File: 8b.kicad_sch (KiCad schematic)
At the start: 51 parts, among them J1 AudioJack2, J11 AudioJack3, J2 AudioJack2, J3 AudioJack2, J4 AudioJack2, J5 AudioJack2, J6 AudioJack2, J7 AudioJack2, J8 AudioJack2, Q1 2N3904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

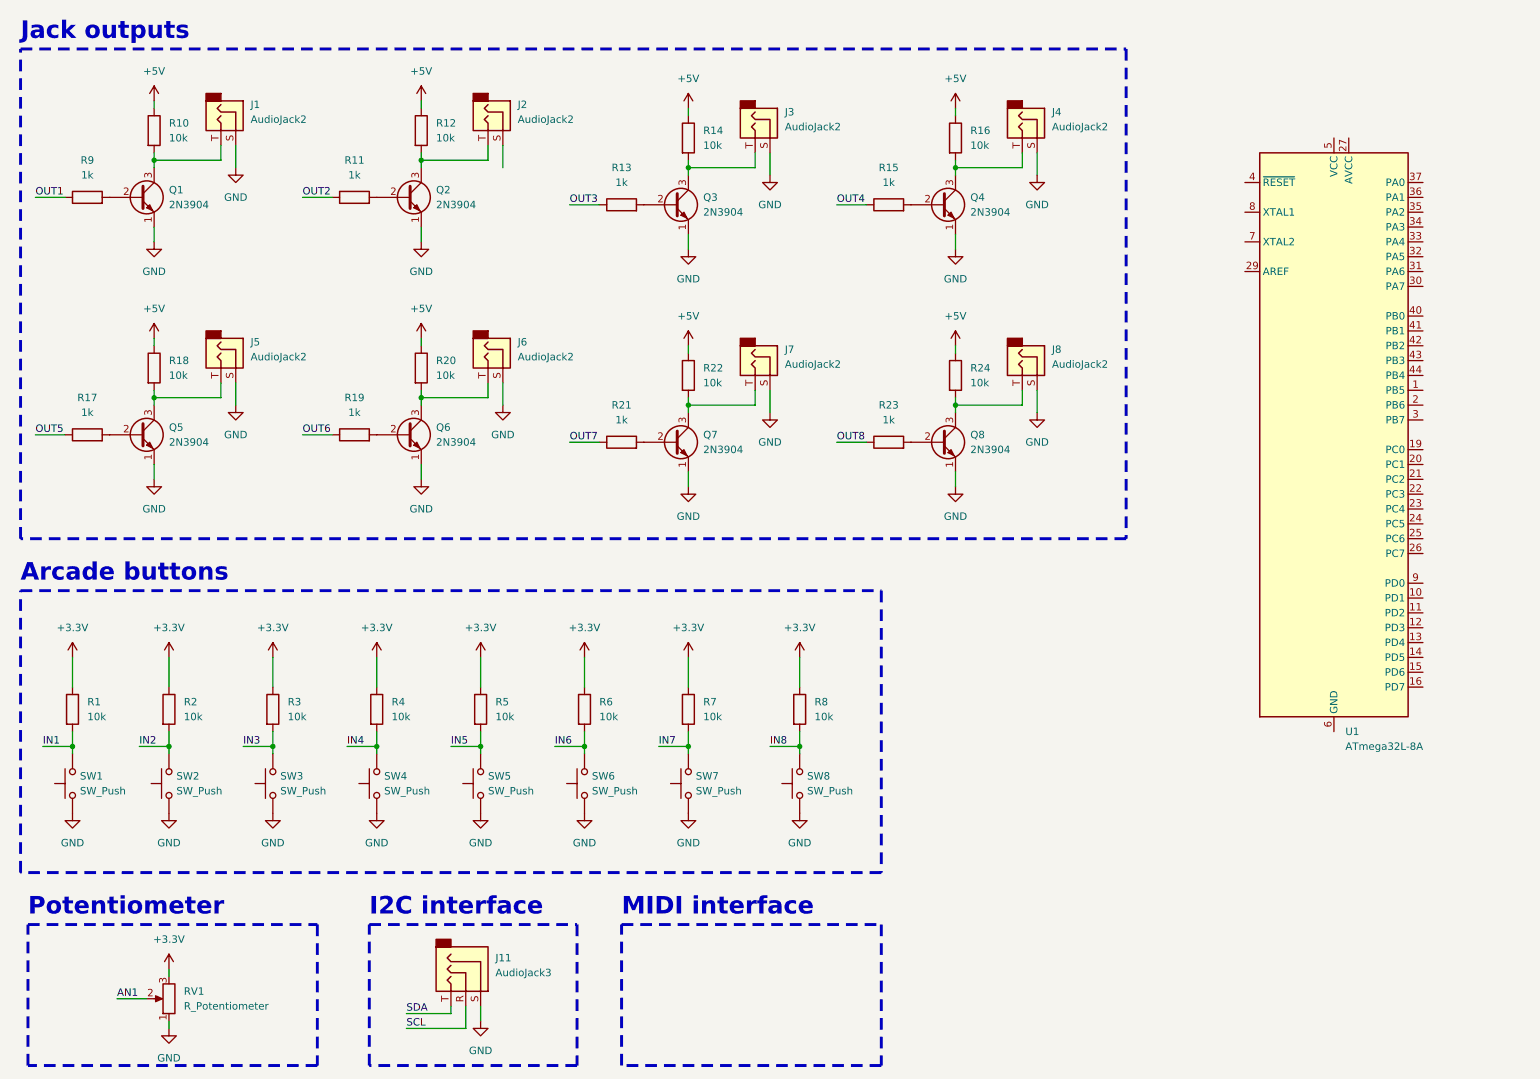
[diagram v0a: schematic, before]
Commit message: Add i2c interface & MIDI interface
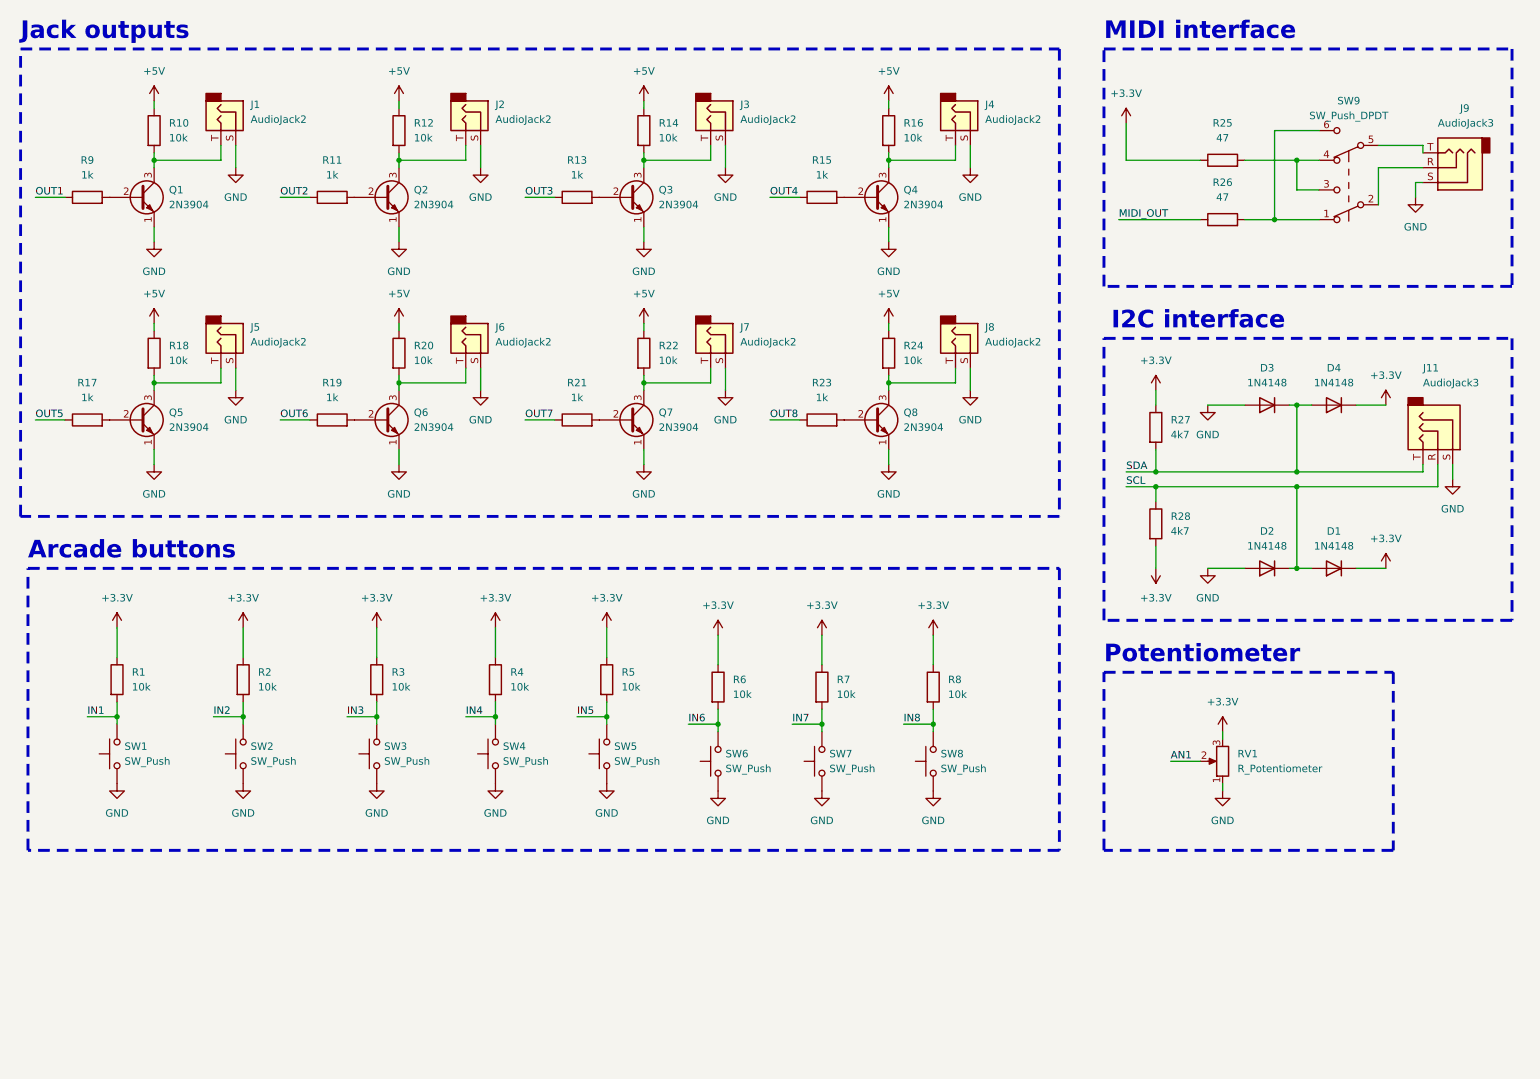
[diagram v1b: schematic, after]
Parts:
- removed U1: ATmega32L-8A, Package_QFP:TQFP-44_10x10mm_P0.8mm, symbol MCU_Microchip_ATmega:ATmega32L-8A
- added D1, D2, D3, D4: 1N4148, Diode_THT:D_DO-35_SOD27_P7.62mm_Horizontal, symbol Diode:1N4148
- added J9: AudioJack3, symbol Connector_Audio:AudioJack3
- added R25, R26: 47, symbol Device:R
- added R27, R28: 4k7, symbol Device:R
- added SW9: SW_Push_DPDT, symbol Switch:SW_Push_DPDT
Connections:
- net +3.3V: now also D1.1 (K), D4.1 (K), R25.1, R27.1, R28.2
- net GND: now also J2.S, D2.2 (A), D3.2 (A), J9.S
- net SCL: now also D1.2 (A), D2.1 (K), R28.1
- net SDA: now also D3.1 (K), D4.2 (A), R27.2
- new net: R26.2, SW9.1 (A), SW9.6 (C)
- new net: J9.R, SW9.2 (B)
- new net: J9.T, SW9.5 (B)
- new net: R25.2, SW9.3 (C), SW9.4 (A)
- new net MIDI_OUT: R26.1
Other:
- moved on the sheet: J11, J2, J3, J4, J5, J6, J7, J8, Q2, Q3, Q4, Q5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

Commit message: Update schem
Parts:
- added U1: Pico, RPi_Pico:RPi_Pico_SMD_TH, symbol RPi Pico:Pico
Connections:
- net +3.3V: now also R27.2, R28.1, U1.36 (3V3); no longer R27.1, R28.2
- net GND: now also U1.3 (GND), U1.42 (GND)
- net SCL: no longer R28.1
- net SDA: now also R27.1, R28.2; no longer R27.2
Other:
- note added: "Control"
- moved on the sheet: D1, D2, D3, D4, J11, J9, R1, R2, R25, R26, R27, R28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

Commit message: Update submodules & schematic
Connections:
- net +5V: now also U1.40 (VBUS)
- net AN1: now also U1.32 (GPIO27_ADC1)
- net GND: now also U1.13 (GND), U1.18 (GND), U1.23 (GND), U1.28 (GND), U1.33 (AGND), U1.38 (GND), U1.8 (GND)
- net IN1: now also U1.9 (GPIO6)
- net IN2: now also U1.10 (GPIO7)
- net IN3: now also U1.11 (GPIO8)
- net IN4: now also U1.12 (GPIO9)
- net IN5: now also U1.14 (GPIO10)
- net IN6: now also U1.15 (GPIO11)
- net IN7: now also U1.16 (GPIO12)
- net IN8: now also U1.17 (GPIO13)
- net MIDI_OUT: now also U1.1 (GPIO0)
- net OUT1: now also U1.19 (GPIO14)
- net OUT2: now also U1.20 (GPIO15)
- net OUT3: now also U1.21 (GPIO16)
- net OUT4: now also U1.22 (GPIO17)
- net OUT5: now also U1.24 (GPIO18)
- net OUT6: now also U1.25 (GPIO19)
- net OUT7: now also U1.26 (GPIO20)
- net OUT8: now also U1.27 (GPIO21)
- net SCL: now also U1.7 (GPIO5)
- net SDA: now also U1.6 (GPIO4)
- no-connect marks 0 -> 12
